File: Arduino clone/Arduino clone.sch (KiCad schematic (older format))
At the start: 0 parts

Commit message: Symbols
Added project symbols.
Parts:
- added BT?: Battery, symbol Device:Battery
- added C? (x2): C, symbol Device:C
- added C?: CP, symbol Device:CP
- added D?: LED, symbol Device:LED
- added R? (x2): R, symbol Device:R
- added U? (x2): 24LC1025, symbol Memory_EEPROM:24LC1025
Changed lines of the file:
@@
 $Descr A4 11693 8268
 encoding utf-8
-Sheet 1 1
+Sheet 1 2
 Title "Arduino clone"
 Date "2020-06-04"
@@
 Comment4 ""
 $EndDescr
+$Comp
+L Device:Battery BT?
+U 1 1 5ED99AAE
+P 1975 3875
+F 0 "BT?" H 2083 3921 50  0000 L CNN
+F 1 "Battery" H 2083 3830 50  0000 L CNN
+F 2 "" V 1975 3935 50  0001 C CNN
+F 3 "~" V 1975 3935 50  0001 C CNN
+	1    1975 3875
+	1    0    0    -1
+$EndComp
+$Comp
+L Device:C C?
+U 1 1 5ED9A7B7
+P 2575 4500
+F 0 "C?" H 2690 4546 50  0000 L CNN
+F 1 "C" H 2690 4455 50  0000 L CNN
+F 2 "" H 2613 4350 50  0001 C CNN
+F 3 "~" H 2575 4500 50  0001 C CNN
+	1    2575 4500
+	1    0    0    -1
+$EndComp
+$Comp
+L Device:C C?
+U 1 1 5ED9AA2C
+P 2575 3800
+F 0 "C?" H 2690 3846 50  0000 L CNN
+F 1 "C" H 2690 3755 50  0000 L CNN
+F 2 "" H 2613 3650 50  0001 C CNN
+F 3 "~" H 2575 3800 50  0001 C CNN
+	1    2575 3800
+	1    0    0    -1
+$EndComp
+$Comp
+L Device:CP C?
+U 1 1 5ED9ACE3
+P 3250 4025
+F 0 "C?" H 3368 4071 50  0000 L CNN
+F 1 "CP" H 3368 3980 50  0000 L CNN
+F 2 "" H 3288 3875 50  0001 C CNN
+F 3 "~" H 3250 4025 50  0001 C CNN
+	1    3250 4025
+	1    0    0    -1
+$EndComp
+$Comp
+L Device:LED D?
+U 1 1 5ED9B092
+P 4175 3975
+F 0 "D?" H 4168 4191 50  0000 C CNN
+F 1 "LED" H 4168 4100 50  0000 C CNN
+F 2 "" H 4175 3975 50  0001 C CNN
+F 3 "~" H 4175 3975 50  0001 C CNN
+	1    4175 3975
+	1    0    0    -1
+$EndComp
+$Comp
+L Device:R R?
+U 1 1 5ED9B3B8
+P 4825 4375
+F 0 "R?" H 4895 4421 50  0000 L CNN
+F 1 "R" H 4895 4330 50  0000 L CNN
+F 2 "" V 4755 4375 50  0001 C CNN
+F 3 "~" H 4825 4375 50  0001 C CNN
+	1    4825 4375
+	1    0    0    -1
+$EndComp
+$Comp
+L Device:R R?
+U 1 1 5ED9B729
+P 4825 3825
+F 0 "R?" H 4895 3871 50  0000 L CNN
+F 1 "R" H 4895 3780 50  0000 L CNN
+F 2 "" V 4755 3825 50  0001 C CNN
+F 3 "~" H 4825 3825 50  0001 C CNN
+	1    4825 3825
+	1    0    0    -1
+$EndComp
+$Comp
+L Memory_EEPROM:24LC1025 U?
+U 1 1 5ED9BE4E
+P 5700 3675
+F 0 "U?" H 5700 4156 50  0000 C CNN
+F 1 "24LC1025" H 5700 4065 50  0000 C CNN
+F 2 "" H 5700 3675 50  0001 C CNN
+F 3 "http://ww1.microchip.com/downloads/en/DeviceDoc/21941B.pdf" H 5700 3675 50  0001 C CNN
+	1    5700 3675
+	1    0    0    -1
+$EndComp
+$Comp
+L Memory_EEPROM:24LC1025 U?
+U 1 1 5ED9C1AA
+P 5700 4650
+F 0 "U?" H 5700 5131 50  0000 C CNN
+F 1 "24LC1025" H 5700 5040 50  0000 C CNN
+F 2 "" H 5700 4650 50  0001 C CNN
+F 3 "http://ww1.microchip.com/downloads/en/DeviceDoc/21941B.pdf" H 5700 4650 50  0001 C CNN
+	1    5700 4650
+	1    0    0    -1
+$EndComp
+$Sheet
+S 7625 3850 1200 1500
+U 5EDA0AF4
+F0 "Connectors" 50
+F1 "Connectors.sch" 50
+$EndSheet
 $EndSCHEMATC

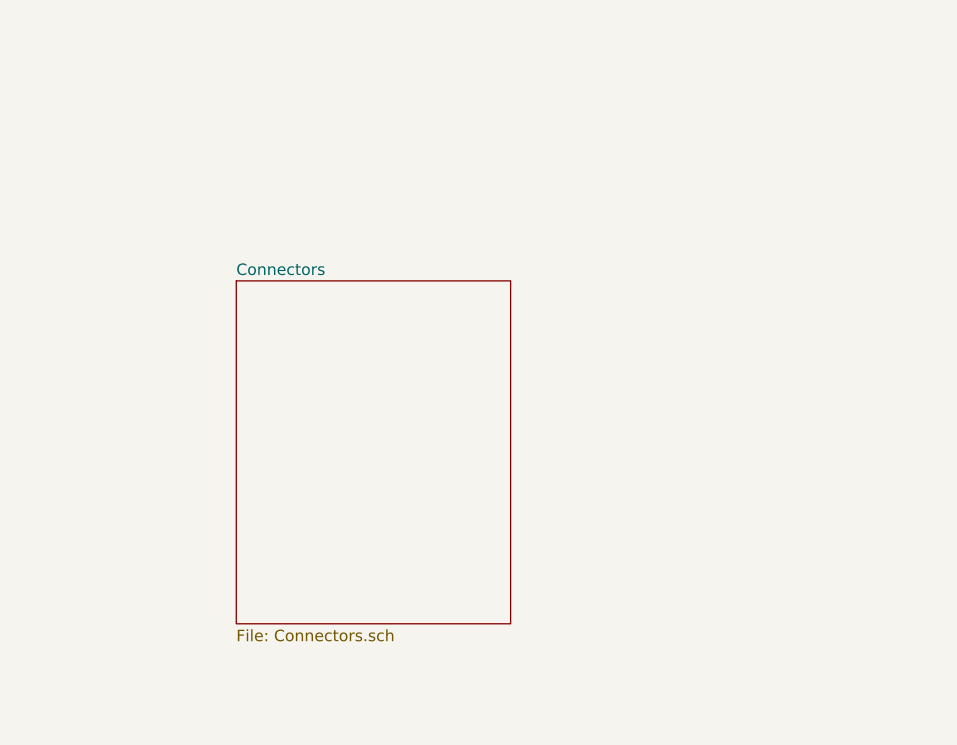
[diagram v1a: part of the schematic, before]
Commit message: ATmega328P-AU symbol.
Added the symbol for the ATmega328P-AU from the DigiKey KiCad library.
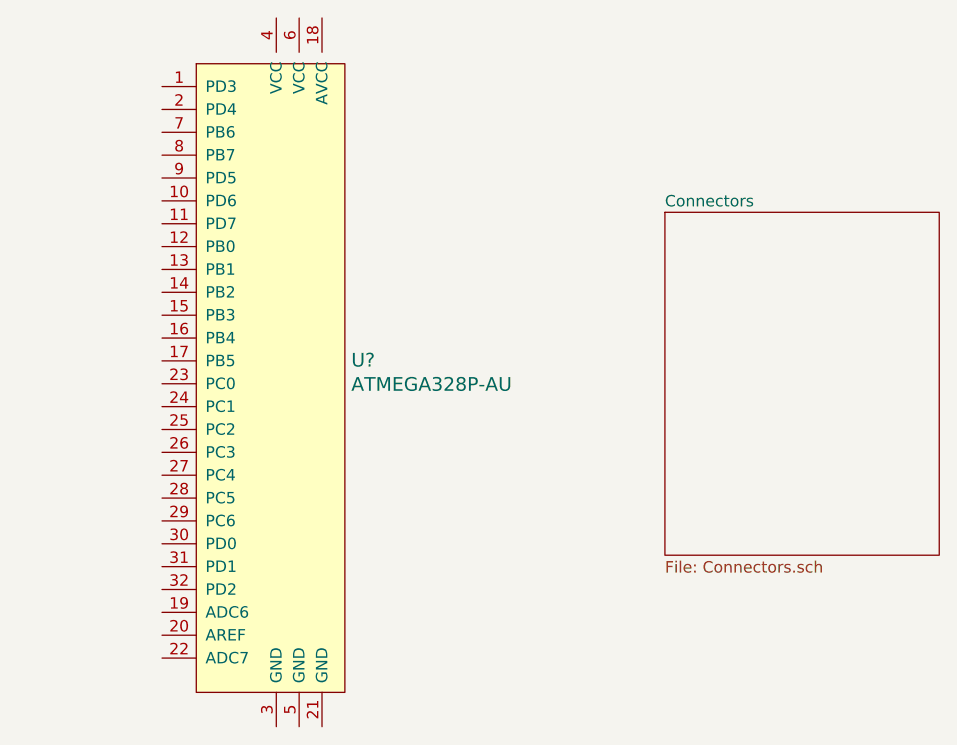
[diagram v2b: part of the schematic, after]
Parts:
- added U?: ATMEGA328P-AU, digikey-footprints:TQFP-32_7x7mm, symbol dk_Embedded-Microcontrollers:ATMEGA328P-AU
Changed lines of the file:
@@
 $EndComp
 $Sheet
-S 7625 3850 1200 1500
+S 9500 3550 1200 1500
 U 5EDA0AF4
 F0 "Connectors" 50
 F1 "Connectors.sch" 50
 $EndSheet
+$Comp
+L dk_Embedded-Microcontrollers:ATMEGA328P-AU U?
+U 1 1 5EDA6E70
+P 7800 4300
+F 0 "U?" H 8128 4403 60  0000 L CNN
+F 1 "ATMEGA328P-AU" H 8128 4297 60  0000 L CNN
+F 2 "digikey-footprints:TQFP-32_7x7mm" H 8000 4500 60  0001 L CNN
+F 3 "http://www.microchip.com/mymicrochip/filehandler.aspx?ddocname=en608326" H 8000 4600 60  0001 L CNN
+F 4 "ATMEGA328P-AU-ND" H 8000 4700 60  0001 L CNN "Digi-Key_PN"
+F 5 "ATMEGA328P-AU" H 8000 4800 60  0001 L CNN "MPN"
+F 6 "Integrated Circuits (ICs)" H 8000 4900 60  0001 L CNN "Category"
+F 7 "Embedded - Microcontrollers" H 8000 5000 60  0001 L CNN "Family"
+F 8 "http://www.microchip.com/mymicrochip/filehandler.aspx?ddocname=en608326" H 8000 5100 60  0001 L CNN "DK_Datasheet_Link"
+F 9 "/product-detail/en/microchip-technology/ATMEGA328P-AU/ATMEGA328P-AU-ND/1832260" H 8000 5200 60  0001 L CNN "DK_Detail_Page"
+F 10 "IC MCU 8BIT 32KB FLASH 32TQFP" H 8000 5300 60  0001 L CNN "Description"
+F 11 "Microchip Technology" H 8000 5400 60  0001 L CNN "Manufacturer"
+F 12 "Active" H 8000 5500 60  0001 L CNN "Status"
+	1    7800 4300
+	1    0    0    -1
+$EndComp
 $EndSCHEMATC

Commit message: Custom RTC symbol
Added custom RTC symbol to schematic.
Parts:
- added U?: DS1337_RYSA, symbol project_3:DS1337_RYSA
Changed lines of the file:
@@
+	1    0    0    -1
+$EndComp
+$Comp
+L project_3:DS1337_RYSA U?
+U 1 1 5EDC0A3E
+P 3575 2825
+F 0 "U?" H 3575 3431 50  0000 C CNN
+F 1 "DS1337_RYSA" H 3575 3340 50  0000 C CNN
+F 2 "" H 3575 2825 50  0001 C CNN
+F 3 "" H 3575 2825 50  0001 C CNN
+	1    3575 2825
 	1    0    0    -1
 $EndComp

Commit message: Crystals
Added missing crystals symbols.
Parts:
- added Y? (x2): Crystal, symbol Device:Crystal
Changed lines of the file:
@@
+	1    0    0    -1
+$EndComp
+$Comp
+L Device:Crystal Y?
+U 1 1 5EDCC86A
+P 4975 5400
+F 0 "Y?" H 4975 5668 50  0000 C CNN
+F 1 "Crystal" H 4975 5577 50  0000 C CNN
+F 2 "" H 4975 5400 50  0001 C CNN
+F 3 "~" H 4975 5400 50  0001 C CNN
+	1    4975 5400
+	1    0    0    -1
+$EndComp
+$Comp
+L Device:Crystal Y?
+U 1 1 5EDCCD58
+P 5025 5950
+F 0 "Y?" H 5025 6218 50  0000 C CNN
+F 1 "Crystal" H 5025 6127 50  0000 C CNN
+F 2 "" H 5025 5950 50  0001 C CNN
+F 3 "~" H 5025 5950 50  0001 C CNN
+	1    5025 5950
 	1    0    0    -1
 $EndComp

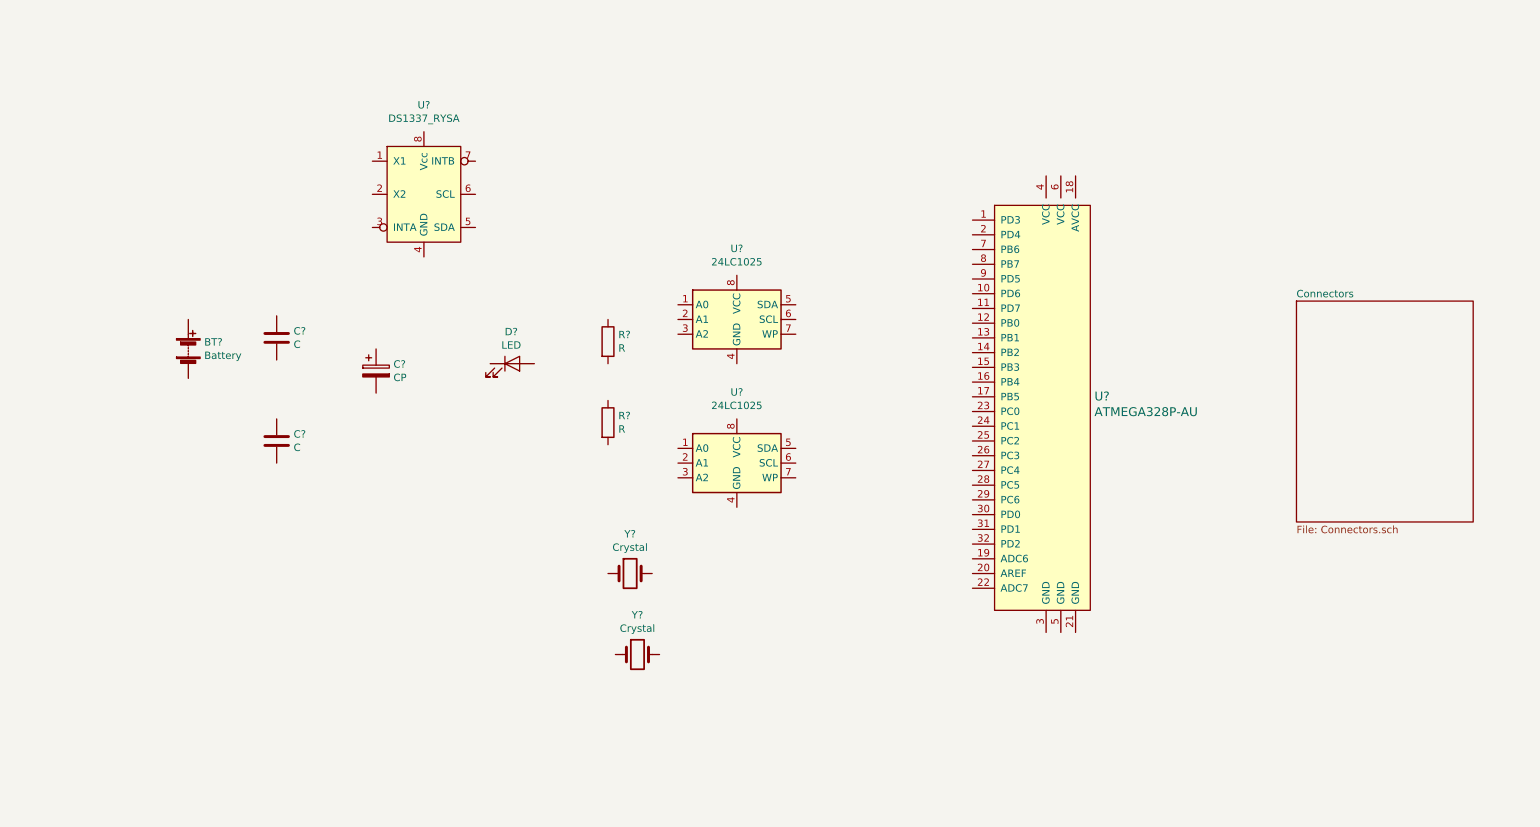
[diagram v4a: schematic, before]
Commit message: Arrange & Annotate
Arranged and annotated symbols in schematics.
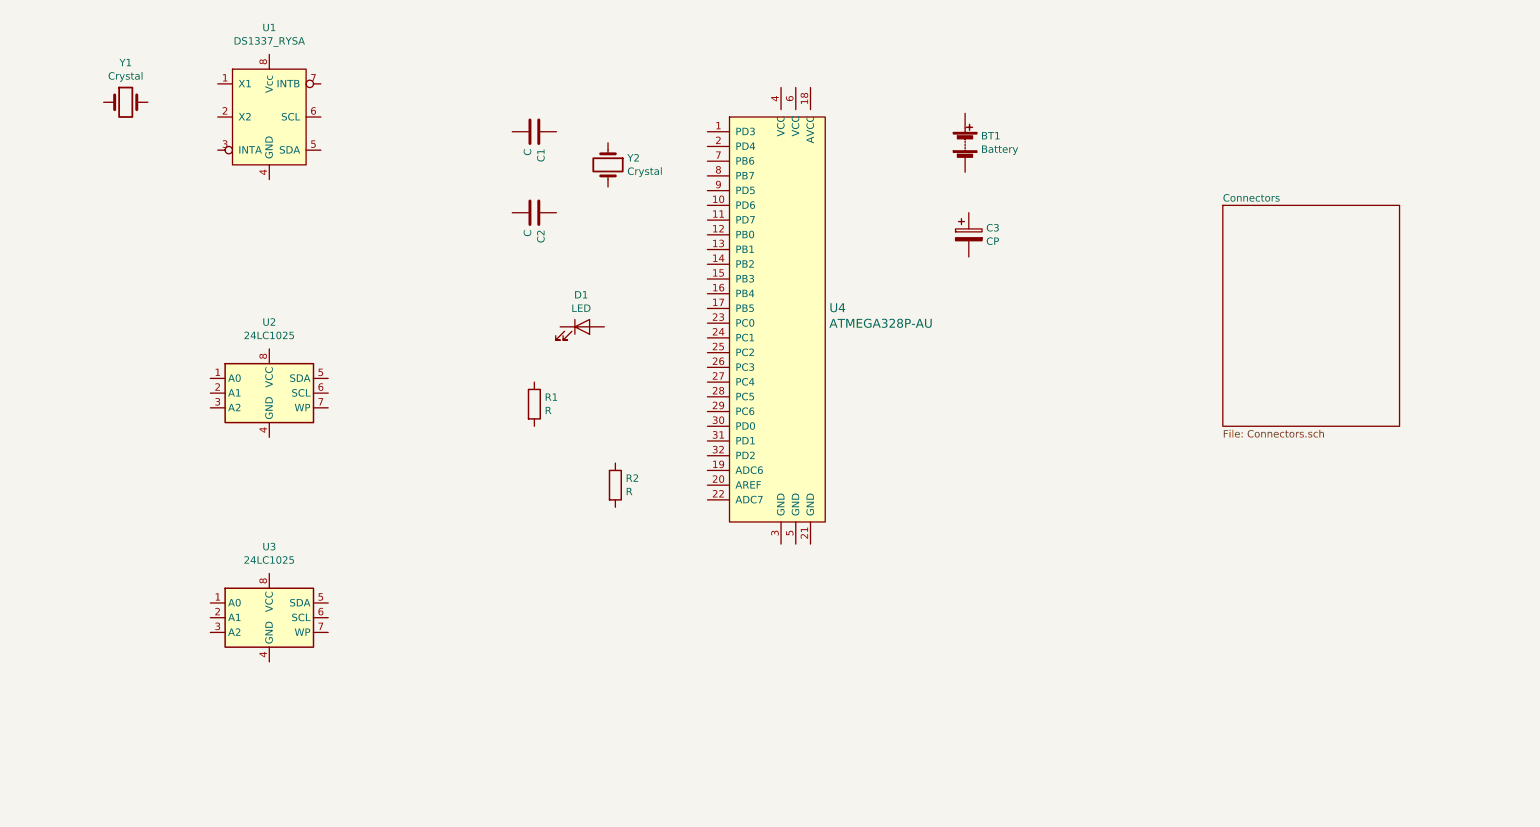
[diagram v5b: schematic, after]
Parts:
- gave numbers to parts that had none: 13
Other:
- moved on the sheet: BT1, C1, C2, C3, D1, R1, R2, U1, U2, U3, U4, Y1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
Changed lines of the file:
@@
 $EndDescr
 $Comp
-L Device:Battery BT?
+L Device:Battery BT1
 U 1 1 5ED99AAE
-P 1975 3875
-F 0 "BT?" H 2083 3921 50  0000 L CNN
-F 1 "Battery" H 2083 3830 50  0000 L CNN
-F 2 "" V 1975 3935 50  0001 C CNN
-F 3 "~" V 1975 3935 50  0001 C CNN
-	1    1975 3875
+P 7250 2475
+F 0 "BT1" H 7358 2521 50  0000 L CNN
+F 1 "Battery" H 7358 2430 50  0000 L CNN
+F 2 "" V 7250 2535 50  0001 C CNN
+F 3 "~" V 7250 2535 50  0001 C CNN
+	1    7250 2475
 	1    0    0    -1
 $EndComp
 $Comp
-L Device:C C?
+L Device:C C1
 U 1 1 5ED9A7B7
-P 2575 4500
-F 0 "C?" H 2690 4546 50  0000 L CNN
-F 1 "C" H 2690 4455 50  0000 L CNN
-F 2 "" H 2613 4350 50  0001 C CNN
-F 3 "~" H 2575 4500 50  0001 C CNN
-	1    2575 4500
+P 4325 2400
+F 0 "C1" H 4440 2446 50  0000 L CNN
+F 1 "C" H 4440 2355 50  0000 L CNN
+F 2 "" H 4363 2250 50  0001 C CNN
+F 3 "~" H 4325 2400 50  0001 C CNN
+	1    4325 2400
+	0    1    1    0
+$EndComp
+$Comp
+L Device:C C2
+U 1 1 5ED9AA2C
+P 4325 2950
+F 0 "C2" H 4440 2996 50  0000 L CNN
+F 1 "C" H 4440 2905 50  0000 L CNN
+F 2 "" H 4363 2800 50  0001 C CNN
+F 3 "~" H 4325 2950 50  0001 C CNN
+	1    4325 2950
+	0    1    1    0
+$EndComp
+$Comp
+L Device:CP C3
+U 1 1 5ED9ACE3
+P 7275 3100
+F 0 "C3" H 7393 3146 50  0000 L CNN
+F 1 "CP" H 7393 3055 50  0000 L CNN
+F 2 "" H 7313 2950 50  0001 C CNN
+F 3 "~" H 7275 3100 50  0001 C CNN
+	1    7275 3100
 	1    0    0    -1
 $EndComp
 $Comp
-L Device:C C?
-U 1 1 5ED9AA2C
-P 2575 3800
-F 0 "C?" H 2690 3846 50  0000 L CNN
-F 1 "C" H 2690 3755 50  0000 L CNN
-F 2 "" H 2613 3650 50  0001 C CNN
-F 3 "~" H 2575 3800 50  0001 C CNN
-	1    2575 3800
+L Device:LED D1
+U 1 1 5ED9B092
+P 4650 3725
+F 0 "D1" H 4643 3941 50  0000 C CNN
+F 1 "LED" H 4643 3850 50  0000 C CNN
+F 2 "" H 4650 3725 50  0001 C CNN
+F 3 "~" H 4650 3725 50  0001 C CNN
+	1    4650 3725
 	1    0    0    -1
 $EndComp
 $Comp
-L Device:CP C?
-U 1 1 5ED9ACE3
-P 3250 4025
-F 0 "C?" H 3368 4071 50  0000 L CNN
-F 1 "CP" H 3368 3980 50  0000 L CNN
-F 2 "" H 3288 3875 50  0001 C CNN
-F 3 "~" H 3250 4025 50  0001 C CNN
-	1    3250 4025
+L Device:R R2
+U 1 1 5ED9B3B8
+P 4875 4800
+F 0 "R2" H 4945 4846 50  0000 L CNN
+F 1 "R" H 4945 4755 50  0000 L CNN
+F 2 "" V 4805 4800 50  0001 C CNN
+F 3 "~" H 4875 4800 50  0001 C CNN
+	1    4875 4800
 	1    0    0    -1
 $EndComp
 $Comp
-L Device:LED D?
-U 1 1 5ED9B092
-P 4175 3975
-F 0 "D?" H 4168 4191 50  0000 C CNN
-F 1 "LED" H 4168 4100 50  0000 C CNN
-F 2 "" H 4175 3975 50  0001 C CNN
-F 3 "~" H 4175 3975 50  0001 C CNN
-	1    4175 3975
+L Device:R R1
+U 1 1 5ED9B729
+P 4325 4250
+F 0 "R1" H 4395 4296 50  0000 L CNN
+F 1 "R" H 4395 4205 50  0000 L CNN
+F 2 "" V 4255 4250 50  0001 C CNN
+F 3 "~" H 4325 4250 50  0001 C CNN
+	1    4325 4250
 	1    0    0    -1
 $EndComp
 $Comp
-L Device:R R?
-U 1 1 5ED9B3B8
-P 4825 4375
-F 0 "R?" H 4895 4421 50  0000 L CNN
-F 1 "R" H 4895 4330 50  0000 L CNN
-F 2 "" V 4755 4375 50  0001 C CNN
-F 3 "~" H 4825 4375 50  0001 C CNN
-	1    4825 4375
+L Memory_EEPROM:24LC1025 U2
+U 1 1 5ED9BE4E
+P 2525 4175
+F 0 "U2" H 2525 4656 50  0000 C CNN
+F 1 "24LC1025" H 2525 4565 50  0000 C CNN
+F 2 "" H 2525 4175 50  0001 C CNN
+F 3 "http://ww1.microchip.com/downloads/en/DeviceDoc/21941B.pdf" H 2525 4175 50  0001 C CNN
+	1    2525 4175
 	1    0    0    -1
 $EndComp
 $Comp
-L Device:R R?
-U 1 1 5ED9B729
-P 4825 3825
-F 0 "R?" H 4895 3871 50  0000 L CNN
-F 1 "R" H 4895 3780 50  0000 L CNN
-F 2 "" V 4755 3825 50  0001 C CNN
-F 3 "~" H 4825 3825 50  0001 C CNN
-	1    4825 3825
-	1    0    0    -1
-$EndComp
-$Comp
-L Memory_EEPROM:24LC1025 U?
-U 1 1 5ED9BE4E
-P 5700 3675
-F 0 "U?" H 5700 4156 50  0000 C CNN
-F 1 "24LC1025" H 5700 4065 50  0000 C CNN
-F 2 "" H 5700 3675 50  0001 C CNN
-F 3 "http://ww1.microchip.com/downloads/en/DeviceDoc/21941B.pdf" H 5700 3675 50  0001 C CNN
-	1    5700 3675
-	1    0    0    -1
-$EndComp
-$Comp
-L Memory_EEPROM:24LC1025 U?
+L Memory_EEPROM:24LC1025 U3
 U 1 1 5ED9C1AA
-P 5700 4650
-F 0 "U?" H 5700 5131 50  0000 C CNN
-F 1 "24LC1025" H 5700 5040 50  0000 C CNN
-F 2 "" H 5700 4650 50  0001 C CNN
-F 3 "http://ww1.microchip.com/downloads/en/DeviceDoc/21941B.pdf" H 5700 4650 50  0001 C CNN
-	1    5700 4650
+P 2525 5700
+F 0 "U3" H 2525 6181 50  0000 C CNN
+F 1 "24LC1025" H 2525 6090 50  0000 C CNN
+F 2 "" H 2525 5700 50  0001 C CNN
+F 3 "http://ww1.microchip.com/downloads/en/DeviceDoc/21941B.pdf" H 2525 5700 50  0001 C CNN
+	1    2525 5700
 	1    0    0    -1
 $EndComp
 $Sheet
-S 9500 3550 1200 1500
+S 9000 2900 1200 1500
 U 5EDA0AF4
 F0 "Connectors" 50
@@
 $EndSheet
 $Comp
-L dk_Embedded-Microcontrollers:ATMEGA328P-AU U?
+L dk_Embedded-Microcontrollers:ATMEGA328P-AU U4
 U 1 1 5EDA6E70
-P 7800 4300
-F 0 "U?" H 8128 4403 60  0000 L CNN
-F 1 "ATMEGA328P-AU" H 8128 4297 60  0000 L CNN
-F 2 "digikey-footprints:TQFP-32_7x7mm" H 8000 4500 60  0001 L CNN
-F 3 "http://www.microchip.com/mymicrochip/filehandler.aspx?ddocname=en608326" H 8000 4600 60  0001 L CNN
-F 4 "ATMEGA328P-AU-ND" H 8000 4700 60  0001 L CNN "Digi-Key_PN"
-F 5 "ATMEGA328P-AU" H 8000 4800 60  0001 L CNN "MPN"
-F 6 "Integrated Circuits (ICs)" H 8000 4900 60  0001 L CNN "Category"
-F 7 "Embedded - Microcontrollers" H 8000 5000 60  0001 L CNN "Family"
-F 8 "http://www.microchip.com/mymicrochip/filehandler.aspx?ddocname=en608326" H 8000 5100 60  0001 L CNN "DK_Datasheet_Link"
-F 9 "/product-detail/en/microchip-technology/ATMEGA328P-AU/ATMEGA328P-AU-ND/1832260" H 8000 5200 60  0001 L CNN "DK_Detail_Page"
-F 10 "IC MCU 8BIT 32KB FLASH 32TQFP" H 8000 5300 60  0001 L CNN "Description"
-F 11 "Microchip Technology" H 8000 5400 60  0001 L CNN "Manufacturer"
-F 12 "Active" H 8000 5500 60  0001 L CNN "Status"
-	1    7800 4300
+P 6000 3700
+F 0 "U4" H 6328 3803 60  0000 L CNN
+F 1 "ATMEGA328P-AU" H 6328 3697 60  0000 L CNN
+F 2 "digikey-footprints:TQFP-32_7x7mm" H 6200 3900 60  0001 L CNN
+F 3 "http://www.microchip.com/mymicrochip/filehandler.aspx?ddocname=en608326" H 6200 4000 60  0001 L CNN
+F 4 "ATMEGA328P-AU-ND" H 6200 4100 60  0001 L CNN "Digi-Key_PN"
+F 5 "ATMEGA328P-AU" H 6200 4200 60  0001 L CNN "MPN"
+F 6 "Integrated Circuits (ICs)" H 6200 4300 60  0001 L CNN "Category"
+F 7 "Embedded - Microcontrollers" H 6200 4400 60  0001 L CNN "Family"
+F 8 "http://www.microchip.com/mymicrochip/filehandler.aspx?ddocname=en608326" H 6200 4500 60  0001 L CNN "DK_Datasheet_Link"
+F 9 "/product-detail/en/microchip-technology/ATMEGA328P-AU/ATMEGA328P-AU-ND/1832260" H 6200 4600 60  0001 L CNN "DK_Detail_Page"
+F 10 "IC MCU 8BIT 32KB FLASH 32TQFP" H 6200 4700 60  0001 L CNN "Description"
+F 11 "Microchip Technology" H 6200 4800 60  0001 L CNN "Manufacturer"
+F 12 "Active" H 6200 4900 60  0001 L CNN "Status"
+	1    6000 3700
 	1    0    0    -1
 $EndComp
 $Comp
-L project_3:DS1337_RYSA U?
+L project_3:DS1337_RYSA U1
 U 1 1 5EDC0A3E
-P 3575 2825
-F 0 "U?" H 3575 3431 50  0000 C CNN
-F 1 "DS1337_RYSA" H 3575 3340 50  0000 C CNN
-F 2 "" H 3575 2825 50  0001 C CNN
-F 3 "" H 3575 2825 50  0001 C CNN
-	1    3575 2825
+P 2525 2300
+F 0 "U1" H 2525 2906 50  0000 C CNN
+F 1 "DS1337_RYSA" H 2525 2815 50  0000 C CNN
+F 2 "" H 2525 2300 50  0001 C CNN
+F 3 "" H 2525 2300 50  0001 C CNN
+	1    2525 2300
 	1    0    0    -1
 $EndComp
 $Comp
-L Device:Crystal Y?
+L Device:Crystal Y1
 U 1 1 5EDCC86A
-P 4975 5400
-F 0 "Y?" H 4975 5668 50  0000 C CNN
-F 1 "Crystal" H 4975 5577 50  0000 C CNN
-F 2 "" H 4975 5400 50  0001 C CNN
-F 3 "~" H 4975 5400 50  0001 C CNN
-	1    4975 5400
+P 1550 2200
+F 0 "Y1" H 1550 2468 50  0000 C CNN
+F 1 "Crystal" H 1550 2377 50  0000 C CNN
+F 2 "" H 1550 2200 50  0001 C CNN
+F 3 "~" H 1550 2200 50  0001 C CNN
+	1    1550 2200
 	1    0    0    -1
 $EndComp
 $Comp
-L Device:Crystal Y?
+L Device:Crystal Y2
 U 1 1 5EDCCD58
-P 5025 5950
-F 0 "Y?" H 5025 6218 50  0000 C CNN
-F 1 "Crystal" H 5025 6127 50  0000 C CNN
-F 2 "" H 5025 5950 50  0001 C CNN
-F 3 "~" H 5025 5950 50  0001 C CNN
-	1    5025 5950
-	1    0    0    -1
+P 4825 2625
+F 0 "Y2" V 4779 2756 50  0000 L CNN
+F 1 "Crystal" V 4870 2756 50  0000 L CNN
+F 2 "" H 4825 2625 50  0001 C CNN
+F 3 "~" H 4825 2625 50  0001 C CNN
+	1    4825 2625
+	0    1    1    0
 $EndComp
 $EndSCHEMATC
